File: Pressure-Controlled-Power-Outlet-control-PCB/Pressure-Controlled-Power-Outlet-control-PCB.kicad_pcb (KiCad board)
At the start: 4 copper layers, 99.1 x 99.1 mm, 14 parts, among them J1 Analog water pressure sensor 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, J2 1017515, J3 1017515, K1 Relay_SPST-NO, K2 Relay_SPST-NO, U1 Pico, U2 LM324, U3 LF50_TO220

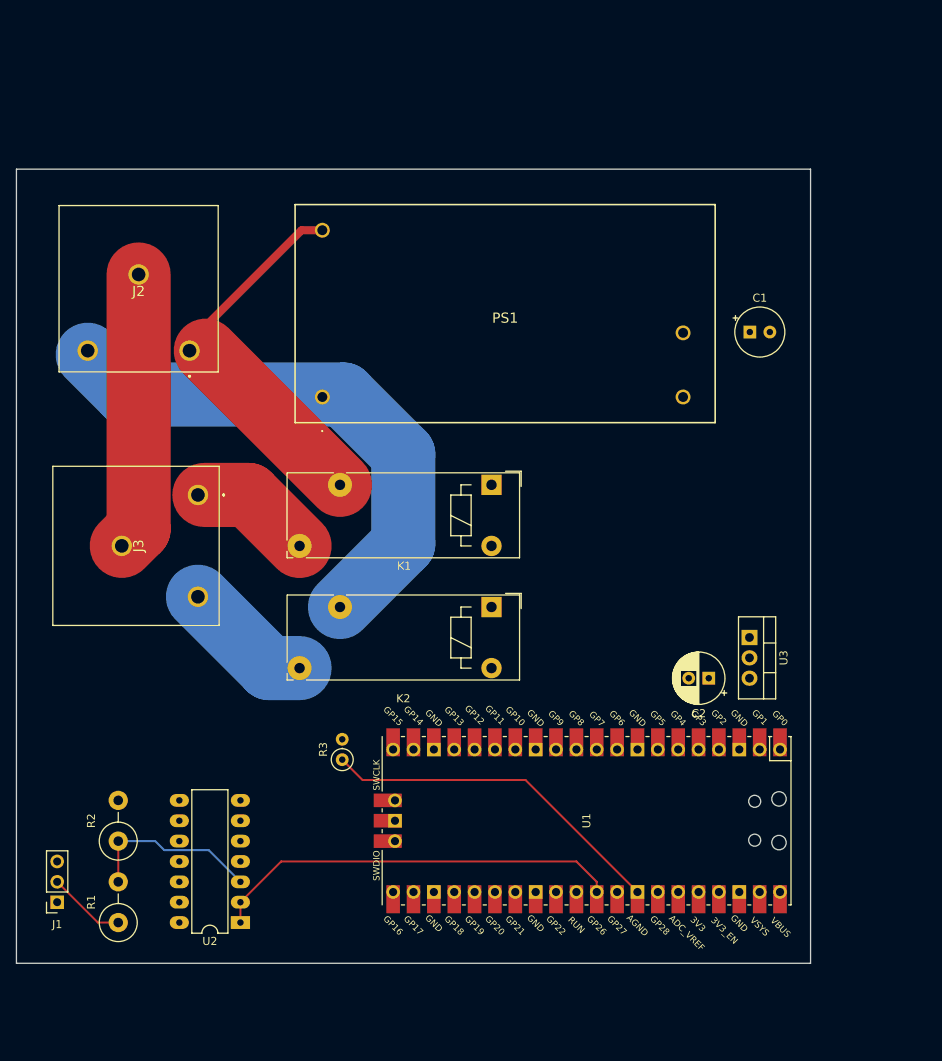
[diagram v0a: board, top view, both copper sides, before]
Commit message: removed onboard power supply and replaced it with an external 24V PSU, and removed High voltage pcb connections as relays have connectors on the top of them
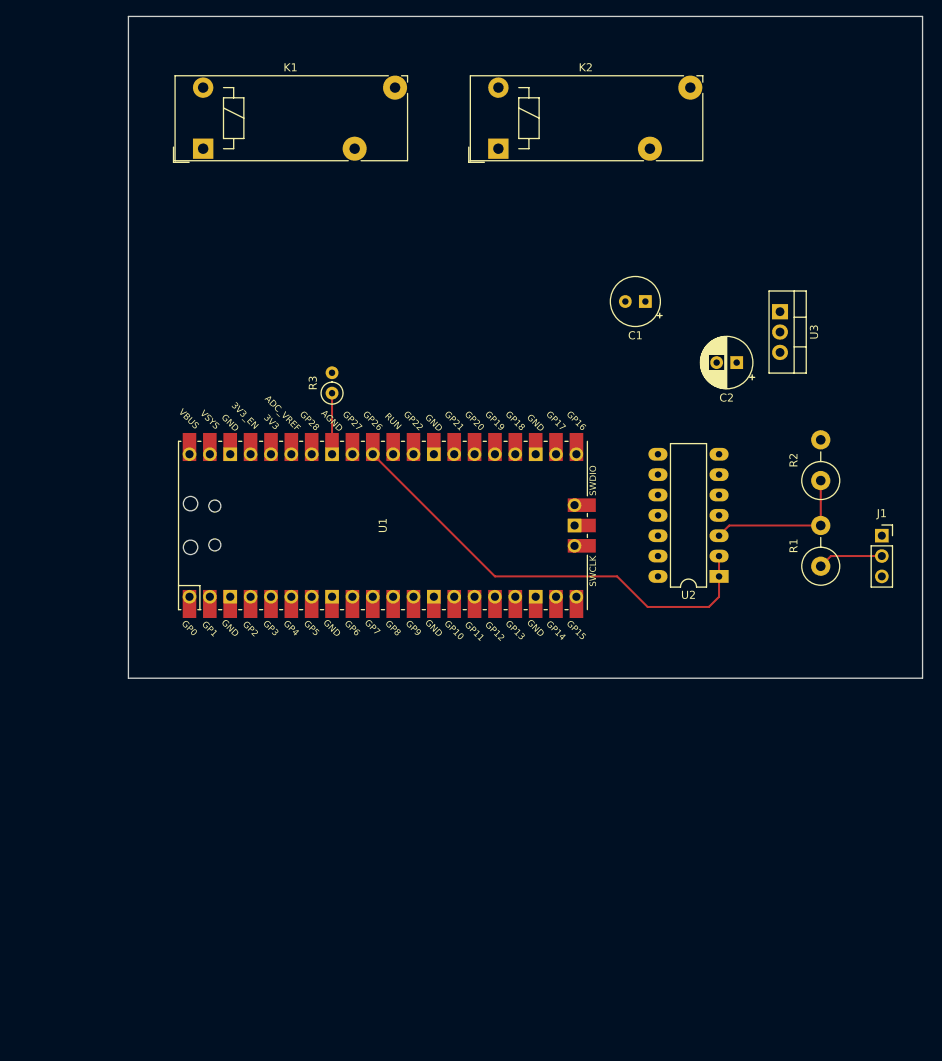
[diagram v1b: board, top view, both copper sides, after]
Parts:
- removed J2, J3: 1017515, Extra:1017515
- removed PS1: MPM-20-12, Extra:MPM2012
- moved J1 112.6 mm to (181.6, 88.9), turned to 0 degrees
- moved R2 98.5 mm to (174.0, 82.0)
- moved R1 98.3 mm to (174.0, 92.7)
- moved U2 73.7 mm to (161.3, 94.0)
- moved K2 57.2 mm to (133.8, 40.6), turned to 0 degrees
- moved K1 55.2 mm to (97.0, 40.6), turned to 0 degrees
- moved R3 45.7 mm to (113.0, 71.1)
- moved U1 44.7 mm to (119.4, 87.6), turned to 90 degrees
- moved U3 40.8 mm to (168.9, 61.0)
- moved C2 39.5 mm to (163.5, 67.3)
- moved C1 13.6 mm to (152.1, 59.7), turned to 180 degrees
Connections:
- net +12V renamed +24V
- K1 pad 11: /Input_Live -> unconnected-(K1-Pad11)
- K1 pad 14: /Output_Live -> unconnected-(K1-Pad14)
- K2 pad 11: /Input_Neutral -> unconnected-(K2-Pad11)
- K2 pad 14: /Output_Neutral -> unconnected-(K2-Pad14)
- U1 pad 40: unconnected-(U1-VBUS-Pad40) -> +5V
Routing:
- net /Input_Neutral: track 67.4 -> 0.00 mm
- net /Input_Live: track 49.1 -> 0.00 mm
- net Net-(U1-AGND): track 43.7 -> 7.62 mm
- net Earth: track 34.7 -> 0.00 mm
- net /Output_Neutral: track 16.4 -> 0.00 mm
- net /Output_Live: track 14.5 -> 0.00 mm
- net /ADC0: track 51.4 -> 56.7 mm
- net Net-(U2A-+): track 22.4 -> 18.8 mm
- net /Water Pressure 5V: track 9.72 -> 8.15 mm
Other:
- board size 99.1 x 99.1 mm -> 99.1 x 82.6 mm

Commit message: wired PCB but the footprint does not match the relay im using so i need to swap the relay :(
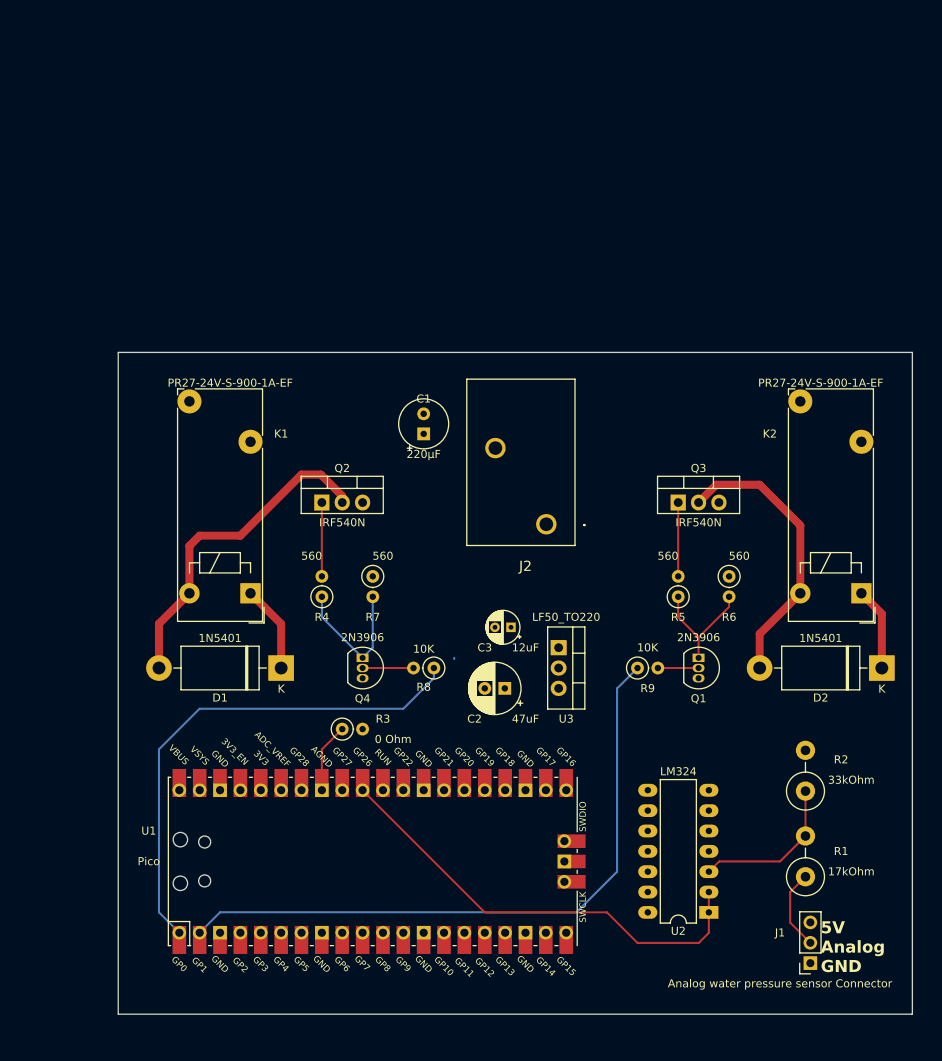
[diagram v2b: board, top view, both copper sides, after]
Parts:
- added C3: 12uF, Capacitor_THT:CP_Radial_D4.0mm_P2.00mm, F.Cu at (135.3, 100.3)
- added D1: 1N5401, Diode_THT:D_DO-201AD_P15.24mm_Horizontal, F.Cu at (106.7, 105.4)
- added D2: 1N5401, Diode_THT:D_DO-201AD_P15.24mm_Horizontal, F.Cu at (181.6, 105.4)
- added J2: 1017514, Extra:1017514, F.Cu at (139.8, 87.5)
- added Q1: 2N3906, Package_TO_SOT_THT:TO-92_Inline, F.Cu at (158.8, 104.1)
- added Q2: IRF540N, Package_TO_SOT_THT:TO-220-3_Vertical, F.Cu at (111.8, 84.8)
- added Q3: IRF540N, Package_TO_SOT_THT:TO-220-3_Vertical, F.Cu at (156.2, 84.8)
- added Q4: 2N3906, Package_TO_SOT_THT:TO-92_Inline, F.Cu at (116.8, 104.1)
- added R4: 560, Resistor_THT:R_Axial_DIN0207_L6.3mm_D2.5mm_P2.54mm_Vertical, F.Cu at (111.8, 96.5)
- added R5: 560, Resistor_THT:R_Axial_DIN0207_L6.3mm_D2.5mm_P2.54mm_Vertical, F.Cu at (156.2, 96.5)
- added R6: 560, Resistor_THT:R_Axial_DIN0207_L6.3mm_D2.5mm_P2.54mm_Vertical, F.Cu at (162.6, 94.0)
- added R7: 560, Resistor_THT:R_Axial_DIN0207_L6.3mm_D2.5mm_P2.54mm_Vertical, F.Cu at (118.1, 94.0)
- added R8: 10K, Resistor_THT:R_Axial_DIN0207_L6.3mm_D2.5mm_P2.54mm_Vertical, F.Cu at (125.7, 105.4)
- added R9: 10K, Resistor_THT:R_Axial_DIN0207_L6.3mm_D2.5mm_P2.54mm_Vertical, F.Cu at (151.1, 105.4)
- K1, K2: value Relay_SPST-NO -> PR27-24V-S-900-1A-EF
- moved K2 71.6 mm to (179.1, 96.1), turned to 90 degrees
- moved K1 55.8 mm to (102.9, 96.1), turned to 90 degrees
- moved J1 54.1 mm to (172.7, 142.2), turned to 180 degrees
- moved U3 50.2 mm to (141.3, 102.9)
- moved C2 49.9 mm to (134.6, 108.0)
- moved U2 41.9 mm to (160.0, 135.9)
- moved R3 41.9 mm to (114.3, 113.0), turned to 0 degrees
- moved U1 41.9 mm to (118.1, 129.5)
- moved R1 38.8 mm to (172.1, 131.4)
- moved R2 38.8 mm to (172.1, 120.8)
- moved C1 32.2 mm to (124.5, 76.2), turned to 90 degrees
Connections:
- K1 pad A1: unconnected-(K1-PadA1) -> +24V
- K1 pad A2: unconnected-(K1-PadA2) -> Net-(D1-A)
- K2 pad A1: unconnected-(K2-PadA1) -> +24V
- K2 pad A2: unconnected-(K2-PadA2) -> Net-(D2-A)
- U1 pad 1: unconnected-(U1-GPIO0-Pad1) -> /Activate_Live
- U1 pad 2: unconnected-(U1-GPIO1-Pad2) -> /Activate_Neutral
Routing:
- net /Activate_Neutral: track 0.00 -> 81.7 mm
- net /Activate_Live: track 0.00 -> 63.2 mm
- net Net-(D1-A): track 0.00 -> 41.5 mm
- net Net-(D2-A): track 0.00 -> 35.6 mm
- net +24V: track 0.00 -> 21.3 mm
- net Net-(Q4-E): track 0.00 -> 17.9 mm
- net Net-(Q1-E): track 0.00 -> 15.3 mm
- net Net-(Q3-G): track 0.00 -> 9.22 mm
- net Net-(Q2-G): track 0.00 -> 9.22 mm
- net Net-(Q4-B): track 0.00 -> 6.35 mm
- net Net-(Q1-B): track 0.00 -> 5.08 mm
- net /Water Pressure 5V: track 8.15 -> 10.1 mm
- net Net-(U1-AGND): track 7.62 -> 8.67 mm
- net Net-(U2A-+): track 18.8 -> 19.5 mm
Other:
- board size 99.1 x 82.6 mm -> 99.1 x 82.5 mm
- board text added: "5V Analog GND"

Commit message: fixed PCB
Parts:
- K1, K2: value PR27-24V-S-900-1A-EF -> T9GV5L24-24; footprint Relay_THT:Relay_1-Form-A_Schrack-RYII_RM5mm -> Extra:T9GV5L2424
- moved K2 18.7 mm to (160.4, 97.5), turned to 0 degrees
- moved K1 9.85 mm to (93.1, 97.5), turned to 0 degrees
- moved R6 9.25 mm to (153.7, 91.4)
- moved R5 8.03 mm to (148.6, 94.0)
- moved R4 8.03 mm to (119.4, 94.0)
- moved Q2 7.62 mm to (119.4, 84.8)
- moved R7 6.84 mm to (124.5, 91.4)
- moved Q3 5.49 mm to (150.8, 83.8), turned to 90 degrees
- moved D1 1.27 mm to (106.7, 104.1)
- moved D2 1.27 mm to (181.6, 104.1)
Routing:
- net Net-(D2-A): track 35.6 -> 58.7 mm
- net +24V: track 21.3 -> 0.00 mm
- net Net-(D1-A): track 41.5 -> 56.7 mm
- net Net-(Q2-G): track 9.22 -> 6.67 mm
- net Net-(Q1-E): track 15.3 -> 17.3 mm
- net Net-(Q4-E): track 17.9 -> 16.3 mm
- net Net-(Q3-G): track 9.22 -> 8.54 mm

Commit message: should be done need to review the board to ensure everything is good
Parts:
- R4, R5, R6, R7: value 560 -> 560 Ohm
- R8, R9: value 10K -> 10KOhm
- moved K2 32.1 mm to (180.3, 72.4), turned to 180 degrees
- moved K1 31.8 mm to (112.6, 72.4), turned to 180 degrees
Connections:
- U1 pad 35: /ADC_Ref -> unconnected-(U1-ADC_VREF-Pad35)
- U2 pad 11: (no net) -> GND
- U2 pad 4: (no net) -> +5V
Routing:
- net Net-(D2-A): track 58.7 -> 30.2 mm
- net Net-(D1-A): track 56.7 -> 39.8 mm
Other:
- board size 99.1 x 82.5 mm -> 100.3 x 82.5 mm
- board text added: "T9GV5L24-24 / T9GS1L24-24"

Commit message: updated parts list with latest parts
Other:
- board text added: "Pressure Controlled Power Outlet control PCB 2024-07-18 V1.1"
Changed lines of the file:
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@@
   (gr_rect (start 86.36 66.04) (end 186.69 148.59)
     (stroke (width 0.1) (type default)) (fill none) (layer "Edge.Cuts"))
+  (gr_text "Pressure Controlled Power Outlet control PCB\n2024-07-18\nV1.1\n" (at 87.63 68.58 180) (layer "B.SilkS")
+    (effects (font (size 2 2) (thickness 0.15)) (justify left bottom mirror))
+  )
   (gr_text "5V\nAnalog\nGND" (at 173.99 143.51) (layer "F.SilkS")
     (effects (font (size 1.5 1.5) (thickness 0.3) bold) (justify left bottom))

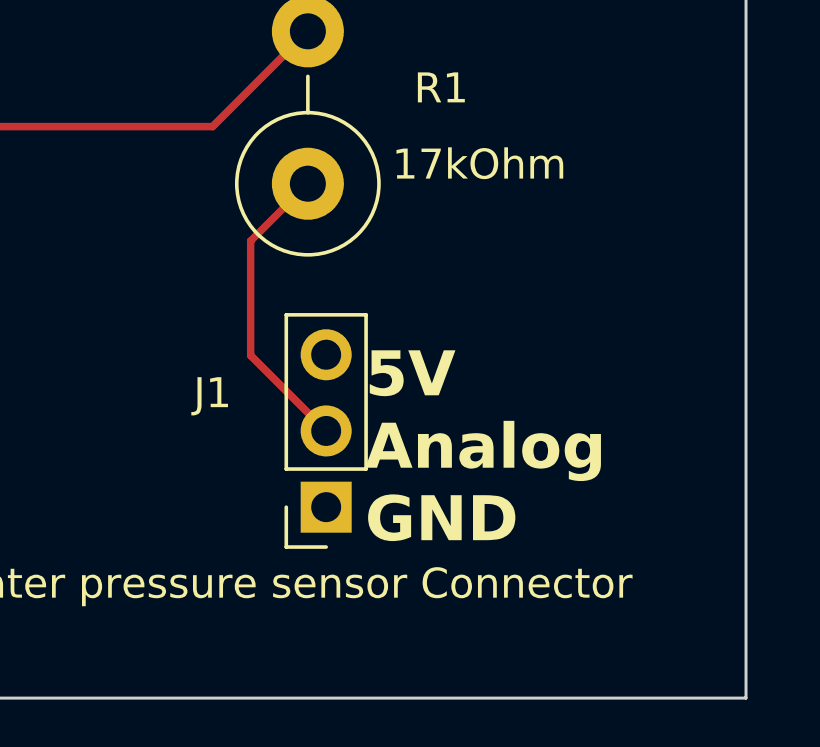
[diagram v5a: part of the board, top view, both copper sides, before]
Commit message: updated to use the sen0257 WPS
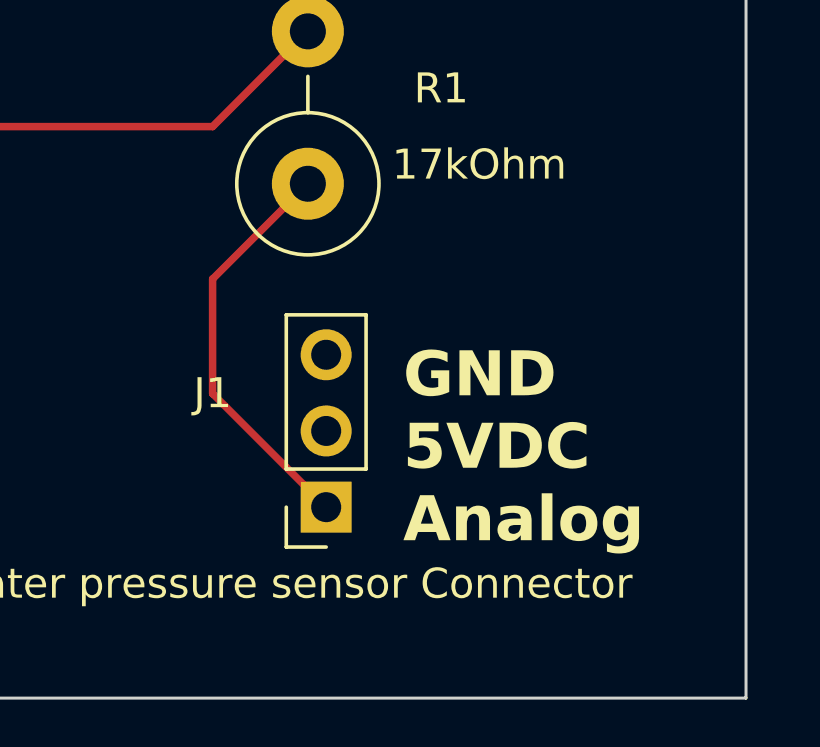
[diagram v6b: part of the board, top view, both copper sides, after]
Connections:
- J1 pad 1: +5V -> /Water Pressure 5V
- J1 pad 2: /Water Pressure 5V -> +5V
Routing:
- net /Water Pressure 5V: track 10.1 -> 13.7 mm
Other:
- board text added: "GND 5VDC Analog"
- board text added: "Pressure Controlled Power Outlet control PCB 2024-07-19 V1.1.1"
- board text removed: "5V Analog GND"
- board text removed: "Pressure Controlled Power Outlet control PCB 2024-07-18 V1.1"
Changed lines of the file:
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@@
     (title "Pressure Controlled Power Outlet")
     (date "2024-07-18")
-    (rev "V1.0")
+    (rev "V1.1.1")
   )
   (layers
@@
       (stroke (width 0.1) (type solid)) (layer "F.Fab"))
     (pad "1" thru_hole rect (at 0 0 180) (size 1.7 1.7) (drill 1) (layers "*.Cu" "*.Mask")
-      (net 33 "+5V") (pinfunction "Pin_1") (pintype "passive"))
+      (net 34 "/Water Pressure 5V") (pinfunction "Pin_1") (pintype "passive"))
     (pad "2" thru_hole oval (at 0 2.54 180) (size 1.7 1.7) (drill 1) (layers "*.Cu" "*.Mask")
-      (net 34 "/Water Pressure 5V") (pinfunction "Pin_2") (pintype "passive"))
+      (net 33 "+5V") (pinfunction "Pin_2") (pintype "passive"))
     (pad "3" thru_hole oval (at 0 5.08 180) (size 1.7 1.7) (drill 1) (layers "*.Cu" "*.Mask")
       (net 1 "GND") (pinfunction "Pin_3") (pintype "passive"))
@@
   (gr_rect (start 86.36 66.04) (end 186.69 148.59)
     (stroke (width 0.1) (type default)) (fill none) (layer "Edge.Cuts"))
-  (gr_text "Pressure Controlled Power Outlet control PCB\n2024-07-18\nV1.1\n" (at 87.63 68.58 180) (layer "B.SilkS")
+  (gr_text "Pressure Controlled Power Outlet control PCB\n2024-07-19\nV1.1.1\n" (at 90.17 107.95 180) (layer "B.SilkS")
     (effects (font (size 2 2) (thickness 0.15)) (justify left bottom mirror))
   )
-  (gr_text "5V\nAnalog\nGND" (at 173.99 143.51) (layer "F.SilkS")
+  (gr_text "GND\n5VDC\nAnalog\n" (at 175.26 143.51) (layer "F.SilkS")
     (effects (font (size 1.5 1.5) (thickness 0.3) bold) (justify left bottom))
   )
@@
   (segment (start 111.76 120.65) (end 111.76 115.57) (width 0.25) (layer "F.Cu") (net 26))
   (segment (start 111.76 115.57) (end 114.3 113.03) (width 0.25) (layer "F.Cu") (net 26))
-  (segment (start 172.695 139.685) (end 170.18 137.17) (width 0.25) (layer "F.Cu") (net 34))
-  (segment (start 170.18 133.35) (end 172.085 131.445) (width 0.25) (layer "F.Cu") (net 34))
-  (segment (start 170.18 137.17) (end 170.18 133.35) (width 0.25) (layer "F.Cu") (net 34))
+  (segment (start 172.085 131.445) (end 168.91 134.62) (width 0.25) (layer "F.Cu") (net 34))
+  (segment (start 168.91 138.44) (end 172.695 142.225) (width 0.25) (layer "F.Cu") (net 34))
+  (segment (start 168.91 134.62) (end 168.91 138.44) (width 0.25) (layer "F.Cu") (net 34))
   (segment (start 172.085 126.365) (end 168.91 129.54) (width 0.25) (layer "F.Cu") (net 35))
   (segment (start 161.31 129.54) (end 160.035 130.815) (width 0.25) (layer "F.Cu") (net 35))
